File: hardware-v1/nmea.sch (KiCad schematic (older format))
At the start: 23 parts, among them P1 CONN_01X20, U10 MCP2562, U11 SN7534051, U12 INA219

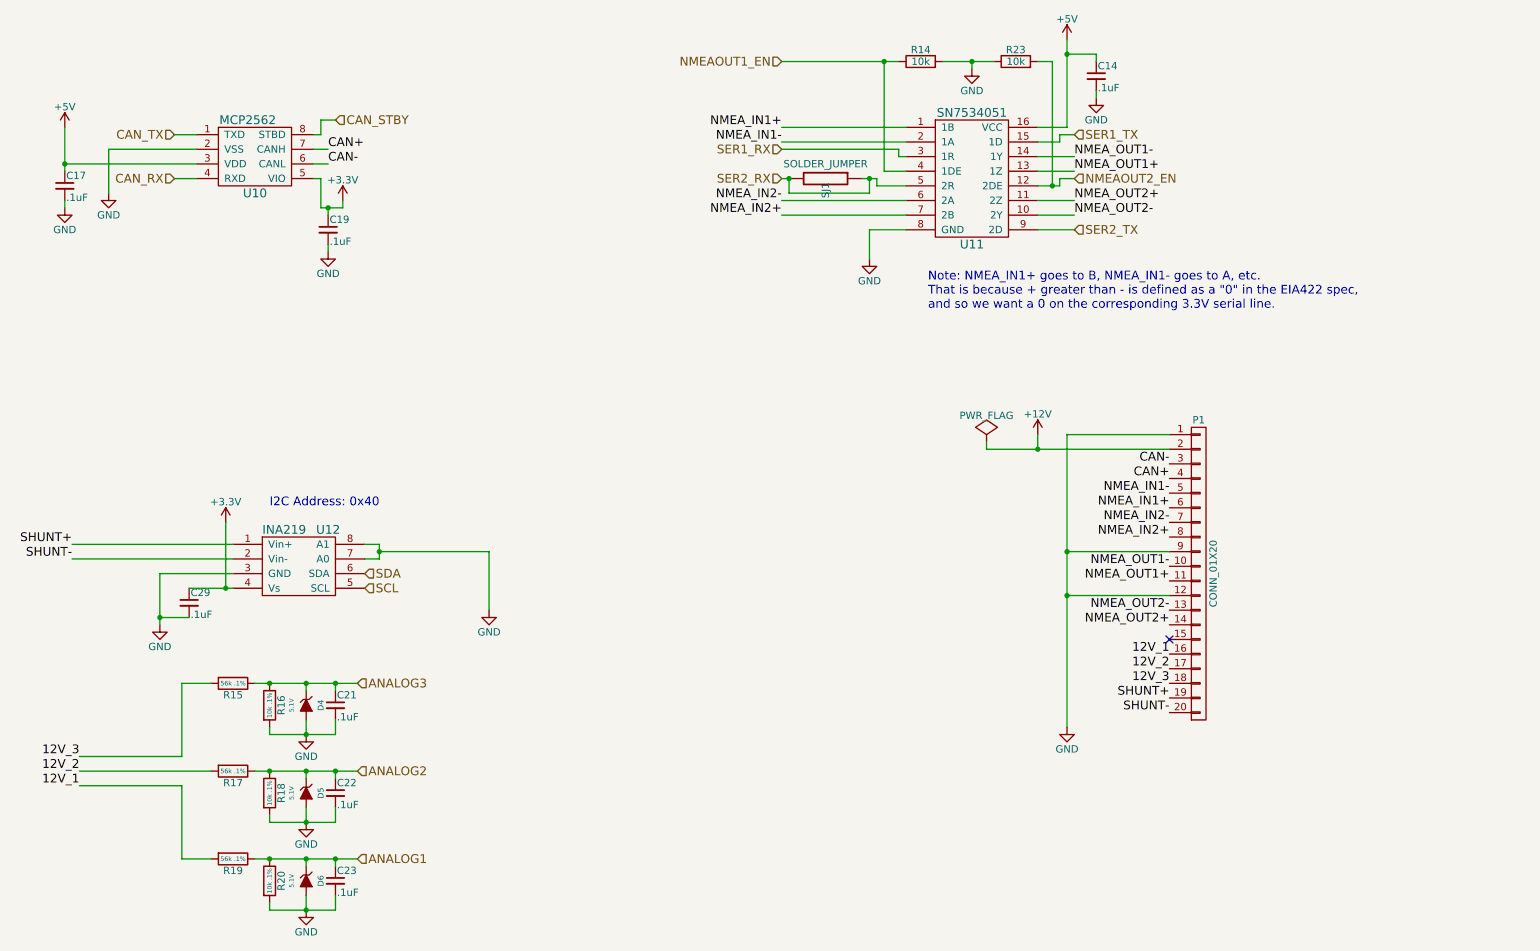
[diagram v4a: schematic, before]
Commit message: Add 10ohms resistor to protect ina219
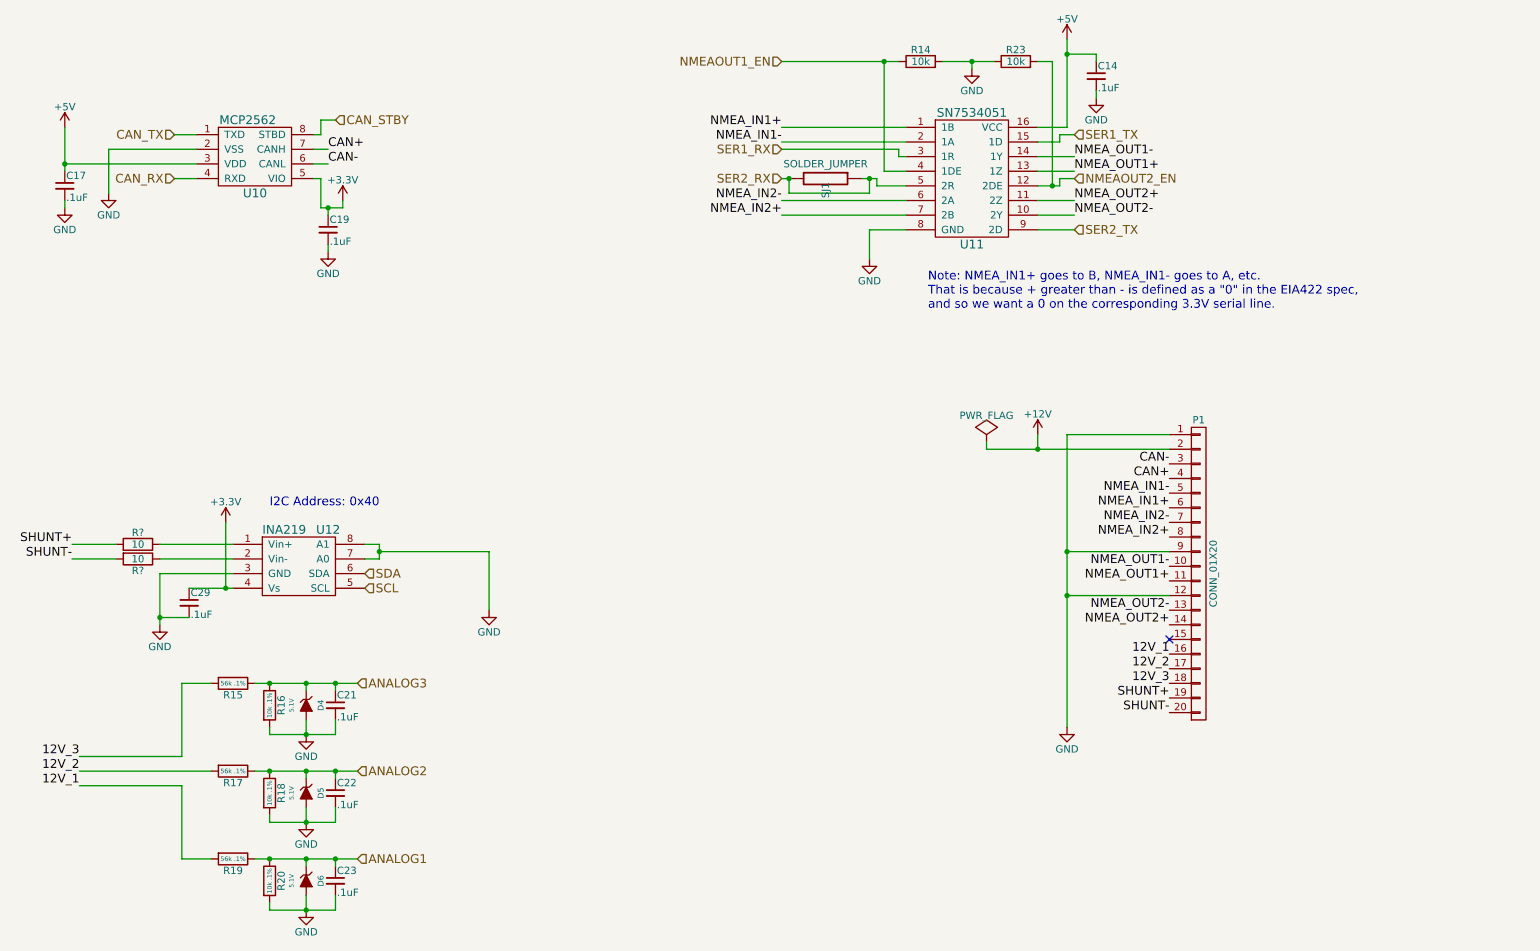
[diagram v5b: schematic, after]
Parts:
- added R? (x2): 10, symbol R
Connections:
- net SHUNT+: now also R?.2; no longer U12.1 (Vin+)
- net SHUNT-: now also R?.2; no longer U12.2 (Vin-)
- new net: R?.1, U12.1 (Vin+)
- new net: R?.1, U12.2 (Vin-)
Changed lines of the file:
@@
 	2400 5500 2600 5500
 Wire Wire Line
-	2900 5500 3000 5500
-Wire Wire Line
-	3000 5500 3250 5500
-Wire Wire Line
-	3250 5500 3450 5500
-Wire Wire Line
-	3450 5500 3600 5500
+	2900 5500 3600 5500
 Connection ~ 3000 5500
 Wire Wire Line
@@
 	3000 5800 3000 5850
 Wire Wire Line
-	3000 5850 3250 5850
-Wire Wire Line
-	3250 5850 3450 5850
+	3000 5850 3450 5850
 Connection ~ 3250 5850
 Wire Wire Line
@@
 	2500 1950 1600 1950
 Wire Wire Line
-	1600 1700 1600 1950
-Wire Wire Line
-	1600 1950 1600 2000
+	1600 1700 1600 2000
 Wire Wire Line
 	3350 1750 3300 1750
 Wire Wire Line
-	3350 2250 3400 2250
-Wire Wire Line
-	3400 2250 3500 2250
+	3350 2250 3500 2250
 Wire Wire Line
 	3400 2300 3400 2250
@@
 	1700 6100 2600 6100
 Wire Wire Line
-	2900 6100 3000 6100
-Wire Wire Line
-	3000 6100 3250 6100
-Wire Wire Line
-	3250 6100 3450 6100
-Wire Wire Line
-	3450 6100 3600 6100
+	2900 6100 3600 6100
 Connection ~ 3000 6100
 Wire Wire Line
@@
 	3000 6400 3000 6450
 Wire Wire Line
-	3000 6450 3250 6450
-Wire Wire Line
-	3250 6450 3450 6450
+	3000 6450 3450 6450
 Connection ~ 3250 6450
 Wire Wire Line
 	2400 6700 2600 6700
 Wire Wire Line
-	2900 6700 3000 6700
-Wire Wire Line
-	3000 6700 3250 6700
-Wire Wire Line
-	3250 6700 3450 6700
-Wire Wire Line
-	3450 6700 3600 6700
+	2900 6700 3600 6700
 Connection ~ 3000 6700
 Wire Wire Line
@@
 	3000 7000 3000 7050
 Wire Wire Line
-	3000 7050 3250 7050
-Wire Wire Line
-	3250 7050 3450 7050
+	3000 7050 3450 7050
 Connection ~ 3250 7050
 Wire Wire Line
@@
 	2400 6200 2400 6700
 Wire Wire Line
-	1650 4550 2750 4550
-Wire Wire Line
-	1650 4650 2750 4650
-Wire Wire Line
 	2750 4750 2250 4750
 Wire Wire Line
-	2250 4750 2250 5050
-Wire Wire Line
-	2250 5050 2250 5100
-Wire Wire Line
-	2450 4850 2700 4850
-Wire Wire Line
-	2700 4850 2750 4850
+	2250 4750 2250 5100
+Wire Wire Line
+	2450 4850 2750 4850
 Wire Wire Line
 	2700 4850 2700 4400
@@
 	3650 4550 3750 4550
 Wire Wire Line
-	3750 4550 3750 4600
-Wire Wire Line
-	3750 4600 3750 4650
+	3750 4550 3750 4650
 Wire Wire Line
 	3750 4650 3650 4650
@@
 	8450 1700 8250 1700
 Wire Wire Line
-	8450 1100 8450 1200
-Wire Wire Line
-	8450 1200 8450 1700
+	8450 1100 8450 1700
 Wire Wire Line
 	8450 1200 8650 1200
@@
 	7100 2400 7100 2600
 Wire Wire Line
-	8250 2100 8350 2100
-Wire Wire Line
-	8350 2100 8400 2100
+	8250 2100 8400 2100
 Wire Wire Line
 	6500 2200 7350 2200
@@
 	7300 1850 6500 1850
 Wire Wire Line
-	6500 1250 7200 1250
-Wire Wire Line
-	7200 1250 7300 1250
+	6500 1250 7300 1250
 Wire Wire Line
 	7200 1250 7200 2000
@@
 Connection ~ 7200 1250
 Wire Wire Line
-	7600 1250 7800 1250
-Wire Wire Line
-	7800 1250 7950 1250
+	7600 1250 7950 1250
 Wire Wire Line
 	7800 1250 7800 1300
@@
 	7150 2050 7150 2100
 Wire Wire Line
-	7050 2050 7100 2050
-Wire Wire Line
-	7100 2050 7150 2050
-Wire Wire Line
-	7900 3900 8250 3900
-Wire Wire Line
-	8250 3900 9150 3900
+	7050 2050 7150 2050
+Wire Wire Line
+	7900 3900 9150 3900
 Wire Wire Line
 	8250 3900 8250 3800
@@
 	8450 4900 9150 4900
 Wire Wire Line
-	8450 3800 8450 4600
-Wire Wire Line
-	8450 4600 8450 4900
-Wire Wire Line
-	8450 4900 8450 5800
+	8450 3800 8450 5800
 Connection ~ 8450 4600
 Connection ~ 8450 4900
@@
 Text Notes 3000 4300 0    60   ~ 0
 I2C Address: 0x40
+$Comp
+L R R?
+U 1 1 56A28792
+P 2100 4550
+F 0 "R?" V 2180 4550 50  0000 C CNN
+F 1 "10" V 2100 4550 50  0000 C CNN
+F 2 "" V 2030 4550 50  0000 C CNN
+F 3 "" H 2100 4550 50  0000 C CNN
+	1    2100 4550
+	0    1    -1   0
+$EndComp
+$Comp
+L R R?
+U 1 1 56A28825
+P 2100 4650
+F 0 "R?" V 2180 4650 50  0000 C CNN
+F 1 "10" V 2100 4650 50  0000 C CNN
+F 2 "" V 2030 4650 50  0000 C CNN
+F 3 "" H 2100 4650 50  0000 C CNN
+	1    2100 4650
+	0    1    1    0
+$EndComp
+Wire Wire Line
+	1650 4550 1950 4550
+Wire Wire Line
+	2250 4550 2750 4550
+Wire Wire Line
+	2750 4650 2250 4650
+Wire Wire Line
+	1950 4650 1650 4650
 $EndSCHEMATC

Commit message: Move SER2 break out pins to aux header
 Add jumper to switch between nmea and aux (instead of solder jump)
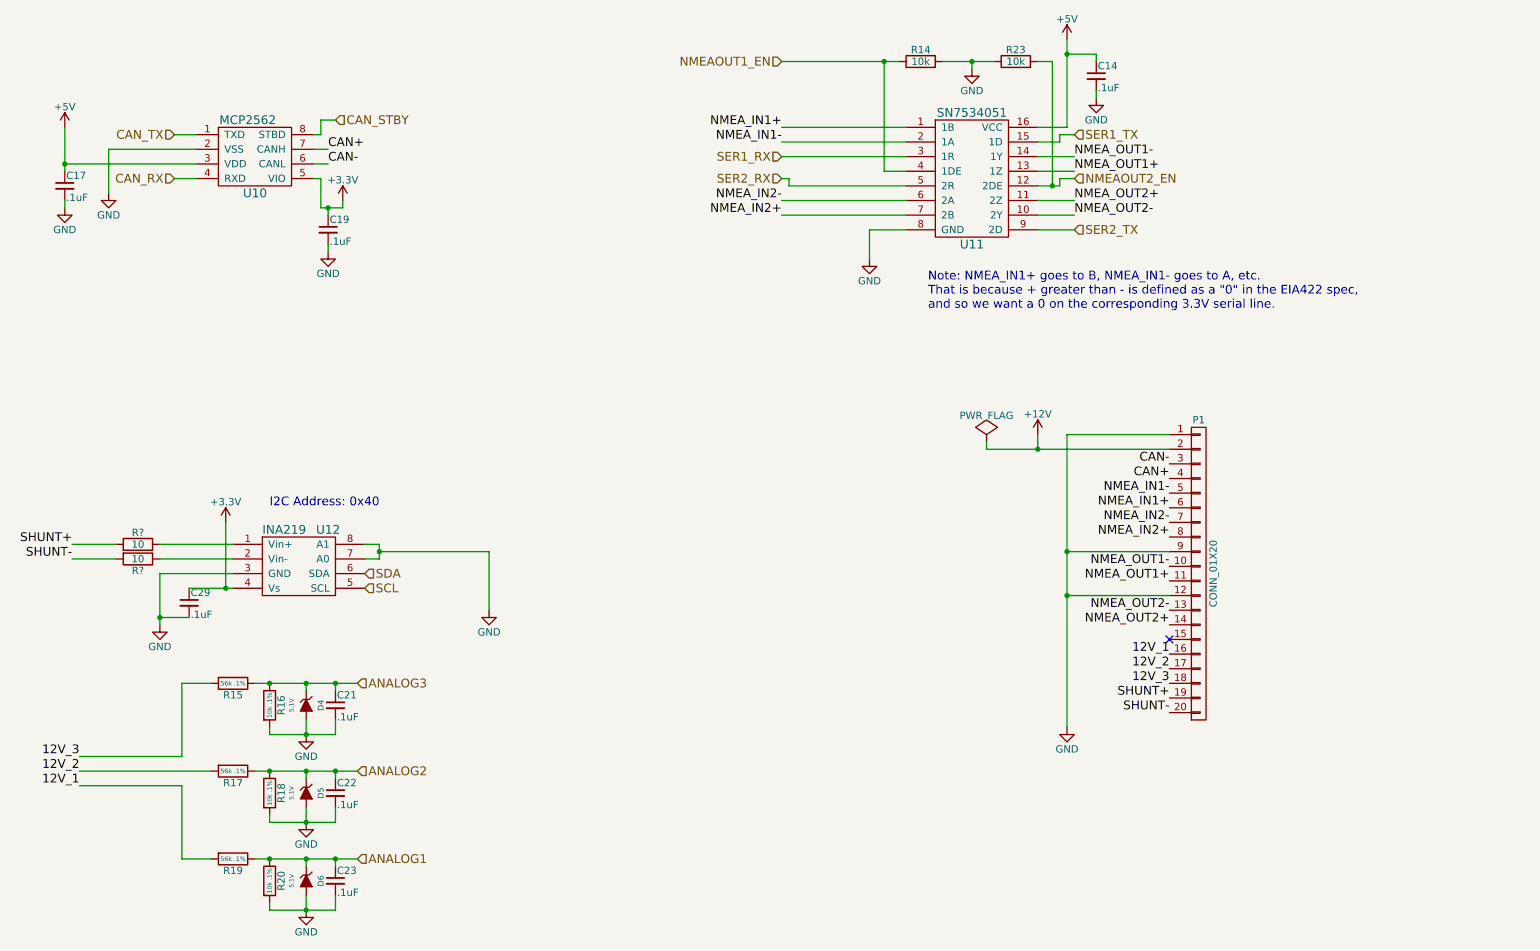
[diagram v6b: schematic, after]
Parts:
- removed SJ1: SOLDER_JUMPER, bb:SolderJumper, symbol SOLDER_JUMPER
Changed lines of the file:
@@
-$EndComp
-$Comp
-L SOLDER_JUMPER SJ1
-U 1 1 56603397
-P 6800 2050
-F 0 "SJ1" H 6880 2050 50  0000 C CNN
-F 1 "SOLDER_JUMPER" V 6700 2050 50  0000 C CNN
-F 2 "bb:SolderJumper" H 6800 2050 60  0001 C CNN
-F 3 "" H 6800 2050 60  0000 C CNN
-	1    6800 2050
-	0    1    1    0
 $EndComp
 $Comp
@@
 Text HLabel 6500 1250 0    60   Input ~ 0
 NMEAOUT1_EN
-Text HLabel 6500 1850 0    60   Input ~ 0
+Text HLabel 6500 1900 0    60   Input ~ 0
 SER1_RX
 $Comp
@@
 	2400 5500 2600 5500
 Wire Wire Line
-	2900 5500 3600 5500
+	2900 5500 3000 5500
+Wire Wire Line
+	3000 5500 3250 5500
+Wire Wire Line
+	3250 5500 3450 5500
+Wire Wire Line
+	3450 5500 3600 5500
 Connection ~ 3000 5500
 Wire Wire Line
@@
 	3000 5800 3000 5850
 Wire Wire Line
-	3000 5850 3450 5850
+	3000 5850 3250 5850
+Wire Wire Line
+	3250 5850 3450 5850
 Connection ~ 3250 5850
 Wire Wire Line
@@
 	2500 1950 1600 1950
 Wire Wire Line
-	1600 1700 1600 2000
+	1600 1700 1600 1950
+Wire Wire Line
+	1600 1950 1600 2000
 Wire Wire Line
 	3350 1750 3300 1750
 Wire Wire Line
-	3350 2250 3500 2250
+	3350 2250 3400 2250
+Wire Wire Line
+	3400 2250 3500 2250
 Wire Wire Line
 	3400 2300 3400 2250
@@
 	1700 6100 2600 6100
 Wire Wire Line
-	2900 6100 3600 6100
+	2900 6100 3000 6100
+Wire Wire Line
+	3000 6100 3250 6100
+Wire Wire Line
+	3250 6100 3450 6100
+Wire Wire Line
+	3450 6100 3600 6100
 Connection ~ 3000 6100
 Wire Wire Line
@@
 	3000 6400 3000 6450
 Wire Wire Line
-	3000 6450 3450 6450
+	3000 6450 3250 6450
+Wire Wire Line
+	3250 6450 3450 6450
 Connection ~ 3250 6450
 Wire Wire Line
 	2400 6700 2600 6700
 Wire Wire Line
-	2900 6700 3600 6700
+	2900 6700 3000 6700
+Wire Wire Line
+	3000 6700 3250 6700
+Wire Wire Line
+	3250 6700 3450 6700
+Wire Wire Line
+	3450 6700 3600 6700
 Connection ~ 3000 6700
 Wire Wire Line
@@
 	3000 7000 3000 7050
 Wire Wire Line
-	3000 7050 3450 7050
+	3000 7050 3250 7050
+Wire Wire Line
+	3250 7050 3450 7050
 Connection ~ 3250 7050
 Wire Wire Line
@@
 	2750 4750 2250 4750
 Wire Wire Line
-	2250 4750 2250 5100
-Wire Wire Line
-	2450 4850 2750 4850
+	2250 4750 2250 5050
+Wire Wire Line
+	2250 5050 2250 5100
+Wire Wire Line
+	2450 4850 2700 4850
+Wire Wire Line
+	2700 4850 2750 4850
 Wire Wire Line
 	2700 4850 2700 4400
@@
 	3650 4550 3750 4550
 Wire Wire Line
-	3750 4550 3750 4650
+	3750 4550 3750 4600
+Wire Wire Line
+	3750 4600 3750 4650
 Wire Wire Line
 	3750 4650 3650 4650
@@
 	8450 1700 8250 1700
 Wire Wire Line
-	8450 1100 8450 1700
+	8450 1100 8450 1200
+Wire Wire Line
+	8450 1200 8450 1700
 Wire Wire Line
 	8450 1200 8650 1200
@@
 	7100 2400 7100 2600
 Wire Wire Line
-	8250 2100 8400 2100
+	8250 2100 8350 2100
+Wire Wire Line
+	8350 2100 8400 2100
 Wire Wire Line
 	6500 2200 7350 2200
@@
 	7350 1900 7300 1900
 Wire Wire Line
-	7300 1900 7300 1850
-Wire Wire Line
-	7300 1850 6500 1850
-Wire Wire Line
-	6500 1250 7300 1250
+	7300 1900 7300 1900
+Wire Wire Line
+	7300 1900 6500 1900
+Wire Wire Line
+	6500 1250 7200 1250
+Wire Wire Line
+	7200 1250 7300 1250
 Wire Wire Line
 	7200 1250 7200 2000
@@
 	7200 2000 7350 2000
 Wire Wire Line
-	7150 2100 7350 2100
+	6550 2100 7350 2100
 Wire Wire Line
 	8250 2400 8500 2400
@@
 Connection ~ 7200 1250
 Wire Wire Line
-	7600 1250 7950 1250
+	7600 1250 7800 1250
+Wire Wire Line
+	7800 1250 7950 1250
 Wire Wire Line
 	7800 1250 7800 1300
@@
 	8400 2050 8400 2100
 Wire Wire Line
-	7150 2050 7150 2100
-Wire Wire Line
-	7050 2050 7150 2050
-Wire Wire Line
-	7900 3900 9150 3900
+	7900 3900 8250 3900
+Wire Wire Line
+	8250 3900 9150 3900
 Wire Wire Line
 	8250 3900 8250 3800
@@
 	8450 4900 9150 4900
 Wire Wire Line
-	8450 3800 8450 5800
+	8450 3800 8450 4600
+Wire Wire Line
+	8450 4600 8450 4900
+Wire Wire Line
+	8450 4900 8450 5800
 Connection ~ 8450 4600
 Connection ~ 8450 4900
@@
 	9150 3800 8450 3800
 Wire Wire Line
-	6550 2050 6500 2050
-Wire Wire Line
-	6550 2050 6550 2150
-Wire Wire Line
-	6550 2150 7100 2150
-Wire Wire Line
-	7100 2150 7100 2050
-Connection ~ 7100 2050
-Connection ~ 6550 2050
+	6500 2050 6550 2050
 Wire Wire Line
 	3350 1750 3350 1650
@@
 Wire Wire Line
 	1950 4650 1650 4650
+Wire Wire Line
+	6550 2050 6550 2100
 $EndSCHEMATC

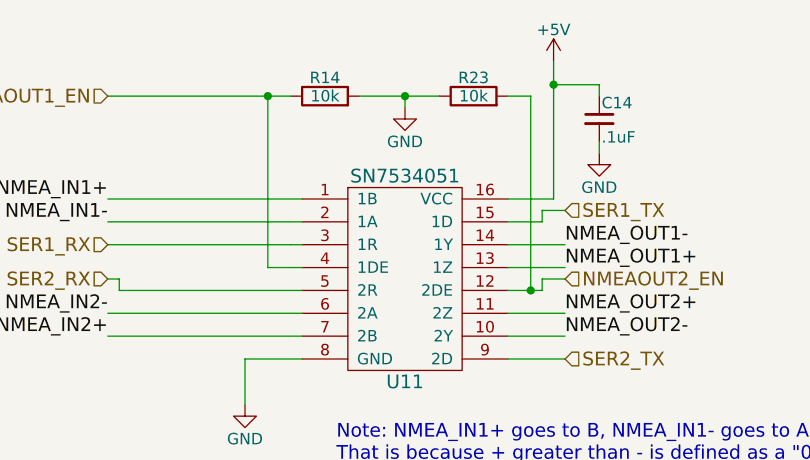
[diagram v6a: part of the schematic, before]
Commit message: Replace SN7534051 by SN65C1168E to save power
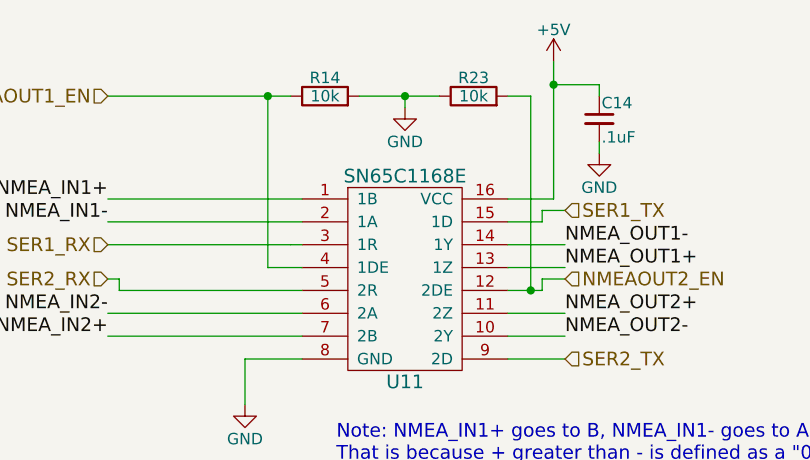
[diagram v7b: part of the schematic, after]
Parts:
- U11: value SN7534051 -> SN65C1168E
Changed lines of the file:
@@
 P 7800 2150
 F 0 "U11" H 7800 1800 60  0000 C CNN
-F 1 "SN7534051" H 7800 2700 60  0000 C CNN
+F 1 "SN65C1168E" H 7800 2700 60  0000 C CNN
 F 2 "bb:SOIC-16_5.6x10.5mm_Pitch1.27mm-HandSolder" H 7800 2150 60  0001 C CNN
 F 3 "" H 7800 2150 60  0000 C CNN
